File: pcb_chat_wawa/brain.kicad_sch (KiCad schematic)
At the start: 16 parts, among them J4 M50-3600742, SW1 SW_Push, SW2 SW_Push, U4 STM32G431CBUx, Y1 Crystal_GND24_Small

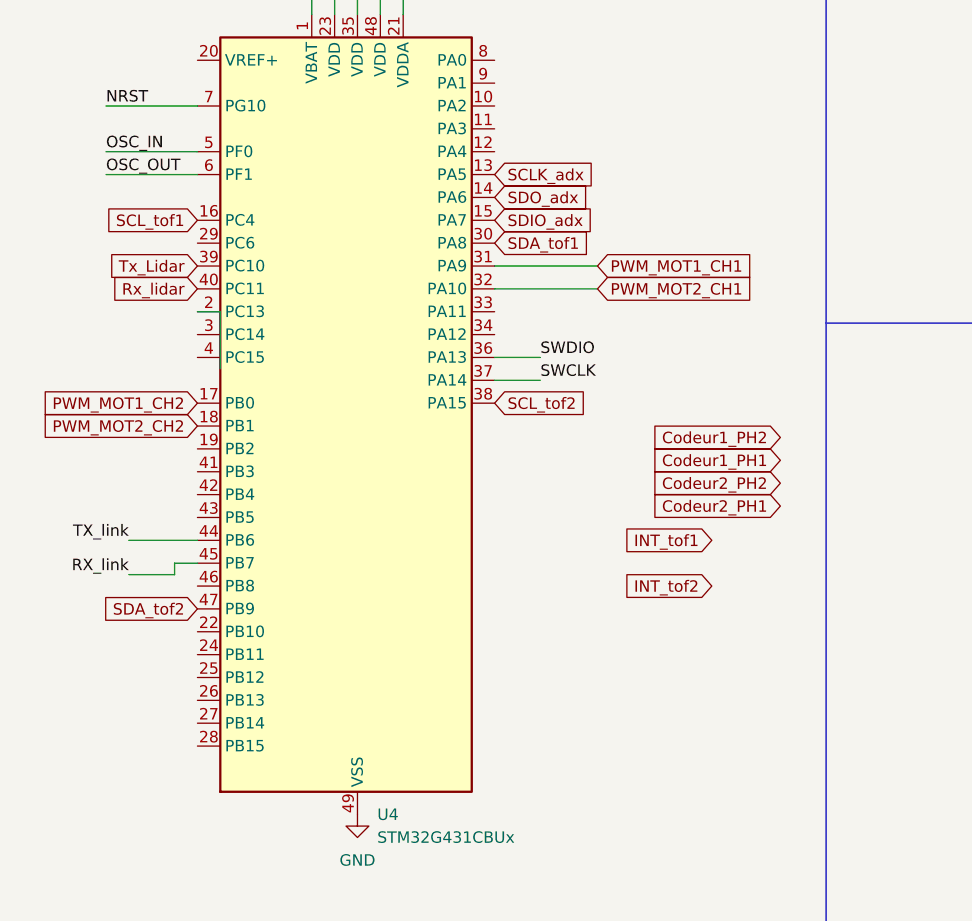
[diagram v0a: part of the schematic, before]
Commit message: modification i2c labels+ajout R à dimmensionner
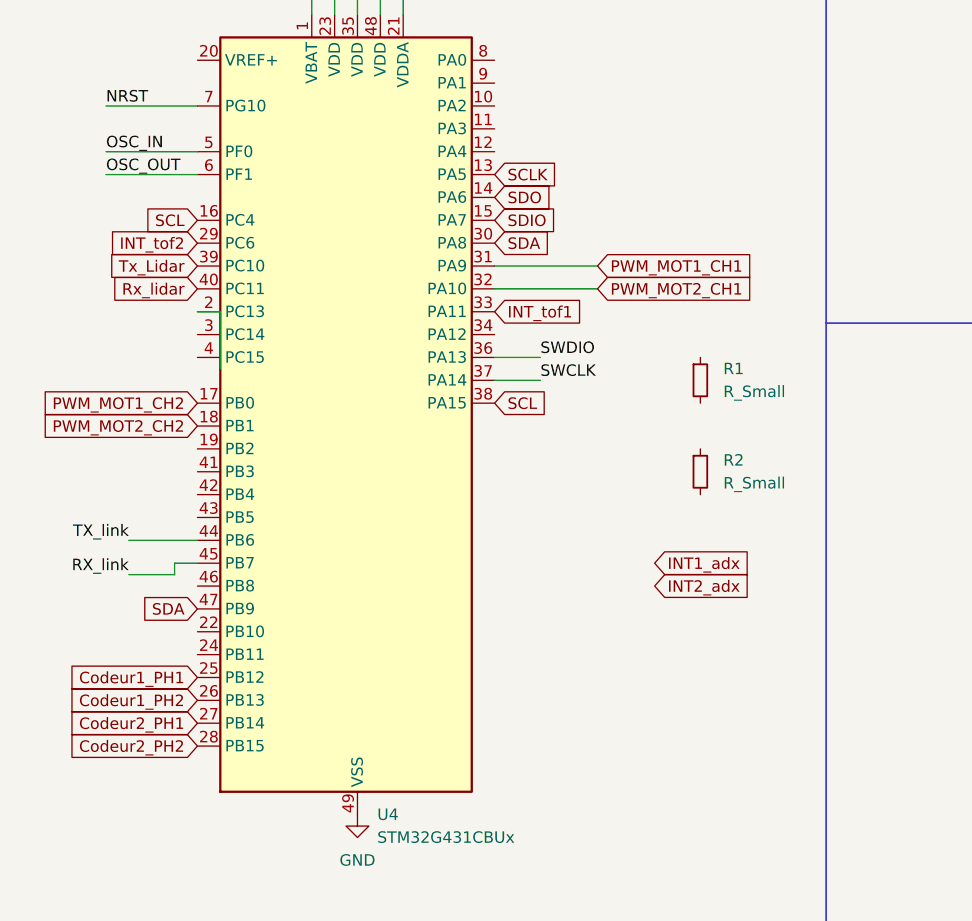
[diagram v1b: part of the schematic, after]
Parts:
- added R1, R2: R_Small, symbol Device:R_Small
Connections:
- net SCL_tof2 is gone; now on net SCL: U4.38 (PA15)
- net SDA_tof2 is gone; now on net SDA: U4.47 (PB9)
- net Codeur1_PH1: now also U4.25 (PB12)
- net Codeur1_PH2: now also U4.26 (PB13)
- net Codeur2_PH1: now also U4.27 (PB14)
- net Codeur2_PH2: now also U4.28 (PB15)
- net INT_tof1: now also U4.33 (PA11)
- net INT_tof2: now also U4.29 (PC6)
- net SCLK_adx renamed SCLK
- net SCL_tof1 renamed SCL
- net SDA_tof1 renamed SDA
- net SDIO_adx renamed SDIO
- net SDO_adx renamed SDO
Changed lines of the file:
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@@
 		)
 	)
-	(global_label "SDO_adx"
+	(global_label "SDO"
 		(shape input)
 		(at 64.77 97.79 0)
@@
 	(global_label "Codeur2_PH1"
 		(shape input)
-		(at 96.52 132.08 180)
+		(at 31.75 156.21 180)
 		(fields_autoplaced yes)
 		(effects
@@
 		)
 		(property "Intersheetrefs" "${INTERSHEET_REFS}"
-			(at 80.9559 132.08 0)
+			(at 16.1859 156.21 0)
 			(effects
 				(font
@@
 		)
 	)
-	(global_label "SCLK_adx"
+	(global_label "INT2_adx"
+		(shape input)
+		(at 82.55 140.97 0)
+		(fields_autoplaced yes)
+		(effects
+			(font
+				(size 1.27 1.27)
+			)
+			(justify left)
+		)
+		(property "Intersheetrefs" "${INTERSHEET_REFS}"
+			(at 89.6476 140.97 0)
+			(effects
+				(font
+					(size 1.27 1.27)
+				)
+				(justify left)
+				(hide yes)
+			)
+		)
+	)
+	(global_label "SCLK"
 		(shape input)
 		(at 64.77 95.25 0)
@@
 		)
 		(property "Intersheetrefs" "${INTERSHEET_REFS}"
-			(at 76.8265 95.25 0)
+			(at 72.5328 95.25 0)
 			(effects
 				(font
@@
 		)
 	)
-	(global_label "SDIO_adx"
+	(global_label "SDIO"
 		(shape input)
 		(at 64.77 100.33 0)
@@
 		)
 	)
-	(global_label "SDA_tof2"
+	(global_label "INT_tof1"
+		(shape input)
+		(at 64.77 110.49 0)
+		(fields_autoplaced yes)
+		(effects
+			(font
+				(size 1.27 1.27)
+			)
+			(justify left)
+		)
+		(property "Intersheetrefs" "${INTERSHEET_REFS}"
+			(at 75.4356 110.49 0)
+			(effects
+				(font
+					(size 1.27 1.27)
+				)
+				(justify left)
+				(hide yes)
+			)
+		)
+	)
+	(global_label "INT1_adx"
+		(shape input)
+		(at 82.55 138.43 0)
+		(fields_autoplaced yes)
+		(effects
+			(font
+				(size 1.27 1.27)
+			)
+			(justify left)
+		)
+		(property "Intersheetrefs" "${INTERSHEET_REFS}"
+			(at 89.6476 138.43 0)
+			(effects
+				(font
+					(size 1.27 1.27)
+				)
+				(justify left)
+				(hide yes)
+			)
+		)
+	)
+	(global_label "SDA"
 		(shape input)
 		(at 31.75 143.51 180)
@@
 		)
 	)
-	(global_label "SDA_tof1"
+	(global_label "SDA"
 		(shape input)
 		(at 64.77 102.87 0)
@@
 	(global_label "Codeur1_PH1"
 		(shape input)
-		(at 96.52 127 180)
+		(at 31.75 151.13 180)
 		(fields_autoplaced yes)
 		(effects
@@
 		)
 		(property "Intersheetrefs" "${INTERSHEET_REFS}"
-			(at 80.9559 127 0)
+			(at 16.1859 151.13 0)
 			(effects
 				(font
@@
 	(global_label "Codeur1_PH2"
 		(shape input)
-		(at 96.52 124.46 180)
+		(at 31.75 153.67 180)
 		(fields_autoplaced yes)
 		(effects
@@
 		)
 		(property "Intersheetrefs" "${INTERSHEET_REFS}"
-			(at 80.9559 124.46 0)
+			(at 16.1859 153.67 0)
 			(effects
 				(font
@@
 		)
 	)
-	(global_label "INT_tof1"
-		(shape input)
-		(at 88.9 135.89 180)
+	(global_label "INT_tof2"
+		(shape input)
+		(at 31.75 102.87 180)
 		(fields_autoplaced yes)
 		(effects
@@
 		)
 		(property "Intersheetrefs" "${INTERSHEET_REFS}"
-			(at 78.2344 135.89 0)
+			(at 21.0844 102.87 0)
 			(effects
 				(font
@@
 		)
 	)
-	(global_label "INT_tof2"
-		(shape input)
-		(at 88.9 140.97 180)
+	(global_label "SCL"
+		(shape input)
+		(at 31.75 100.33 180)
 		(fields_autoplaced yes)
 		(effects
@@
 		)
 		(property "Intersheetrefs" "${INTERSHEET_REFS}"
-			(at 78.2344 140.97 0)
+			(at 20.4797 100.33 0)
 			(effects
 				(font
@@
 		)
 	)
-	(global_label "SCL_tof1"
-		(shape input)
-		(at 31.75 100.33 180)
+	(global_label "Codeur2_PH2"
+		(shape input)
+		(at 31.75 158.75 180)
 		(fields_autoplaced yes)
 		(effects
@@
 		)
 		(property "Intersheetrefs" "${INTERSHEET_REFS}"
-			(at 20.4797 100.33 0)
+			(at 16.1859 158.75 0)
 			(effects
 				(font
@@
 		)
 	)
-	(global_label "Codeur2_PH2"
-		(shape input)
-		(at 96.52 129.54 180)
-		(fields_autoplaced yes)
-		(effects
-			(font
-				(size 1.27 1.27)
-			)
-			(justify right)
-		)
-		(property "Intersheetrefs" "${INTERSHEET_REFS}"
-			(at 80.9559 129.54 0)
-			(effects
-				(font
-					(size 1.27 1.27)
-				)
-				(justify right)
-				(hide yes)
-			)
-		)
-	)
-	(global_label "SCL_tof2"
+	(global_label "SCL"
 		(shape input)
 		(at 64.77 120.65 0)
@@
 	)
 	(symbol
+		(lib_id "Device:R_Small")
+		(at 87.63 128.27 0)
+		(unit 1)
+		(exclude_from_sim no)
+		(in_bom yes)
+		(on_board yes)
+		(dnp no)
+		(fields_autoplaced yes)
+		(property "Reference" "R2"
+			(at 90.17 126.9999 0)
+			(effects
+				(font
+					(size 1.27 1.27)
+				)
+				(justify left)
+			)
+		)
+		(property "Value" "R_Small"
+			(at 90.17 129.5399 0)
+			(effects
+				(font
+					(size 1.27 1.27)
+				)
+				(justify left)
+			)
+		)
+		(property "Footprint" ""
+			(at 87.63 128.27 0)
+			(effects
+				(font
+					(size 1.27 1.27)
+				)
+				(hide yes)
+			)
+		)
+		(property "Datasheet" "~"
+			(at 87.63 128.27 0)
+			(effects
+				(font
+					(size 1.27 1.27)
+				)
+				(hide yes)
+			)
+		)
+		(property "Description" "Resistor, small symbol"
+			(at 87.63 128.27 0)
+			(effects
+				(font
+					(size 1.27 1.27)
+				)
+				(hide yes)
+			)
+		)
+		(pin "2"
+		)
+		(pin "1"
+		)
+		(instances
+			(project "StealthKitty"
+				(path "/23d5732b-7ccb-40aa-85a2-3b18421ac23b/80e324d5-3692-40e2-ae7b-7b2010b2e090"
+					(reference "R2")
+					(unit 1)
+				)
+			)
+		)
+	)
+	(symbol
 		(lib_id "Switch:SW_Push")
 		(at 140.97 125.73 0)
@@
 					(unit 1)
 				)
+			)
+		)
+	)
+	(symbol
+		(lib_id "Device:R_Small")
+		(at 87.63 118.11 0)
+		(unit 1)
+		(exclude_from_sim no)
+		(in_bom yes)
+		(on_board yes)
+		(dnp no)
+		(fields_autoplaced yes)
+		(property "Reference" "R1"
+			(at 90.17 116.8399 0)
+			(effects
+				(font
+					(size 1.27 1.27)
+				)
+				(justify left)
+			)
+		)
+		(property "Value" "R_Small"
+			(at 90.17 119.3799 0)
+			(effects
+				(font
+					(size 1.27 1.27)
+				)
+				(justify left)
+			)
+		)
+		(property "Footprint" ""
+			(at 87.63 118.11 0)
+			(effects
+				(font
+					(size 1.27 1.27)
+				)
+				(hide yes)
+			)
+		)
+		(property "Datasheet" "~"
+			(at 87.63 118.11 0)
+			(effects
+				(font
+					(size 1.27 1.27)
+				)
+				(hide yes)
+			)
+		)
+		(property "Description" "Resistor, small symbol"
+			(at 87.63 118.11 0)
+			(effects
+				(font
+					(size 1.27 1.27)
+				)
+				(hide yes)
+			)
+		)
+		(pin "2"
+		)
+		(pin "1"
+		)
+		(instances
+			(project ""
+				(path "/23d5732b-7ccb-40aa-85a2-3b18421ac23b/80e324d5-3692-40e2-ae7b-7b2010b2e090"
+					(reference "R1")
+					(unit 1)
+				)
